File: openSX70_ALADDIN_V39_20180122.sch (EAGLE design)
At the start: 47 parts, among them J1 GND, Q1 5.8A/30V/35mΩ, Q2 5.8A/30V/35mΩ, U1 ATMEGA328P_TQFP, U3 BH1750FVI-TR, Y1 CSTCE16M0V53-R0

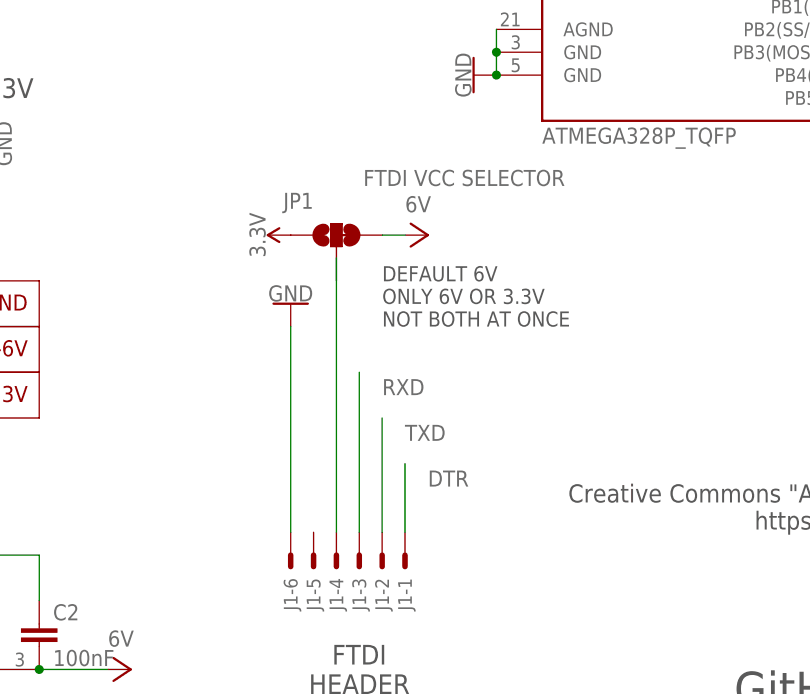
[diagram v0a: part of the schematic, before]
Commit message: New v.3.9 "Aladdin-fpc" is basically Aladdin with the FTDI header changed to the upper left in the form of a flexible cable.
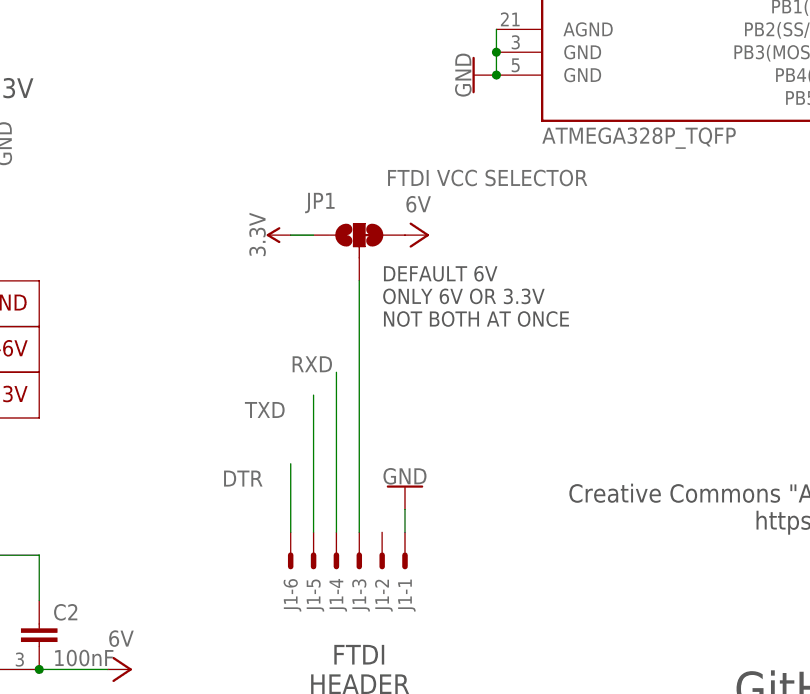
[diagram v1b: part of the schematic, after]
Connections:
- net DTR: now also J1-6.MS; no longer J1-1.MS
- net GND: now also J1-1.MS; no longer J1-6.MS
- net N$27: now also J1-3.MS, JP1.2; no longer J1-4.MS
- net RXD: now also J1-4.MS; no longer J1-3.MS
- net TXD: now also J1-5.MS; no longer J1-2.MS
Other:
- moved on the sheet: JP1
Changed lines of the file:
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@@
 <instance part="U1" gate="U$1" x="170.18" y="96.52"/>
 <instance part="SUPPLY1" gate="G$1" x="121.92" y="53.34" rot="R90"/>
-<instance part="GND1" gate="1" x="121.92" y="45.72" rot="R180"/>
+<instance part="GND1" gate="1" x="134.62" y="25.4" rot="R180"/>
 <instance part="GND2" gate="1" x="218.44" y="88.9" rot="R270"/>
 <instance part="P+1" gate="VCC" x="218.44" y="99.06" rot="R90"/>
@@
 <attribute name="VALUE" x="203.2" y="145.415" size="1.778" layer="96"/>
 </instance>
-<instance part="JP1" gate="G$1" x="127" y="53.34" smashed="yes" rot="R90">
-<attribute name="NAME" x="124.46" y="58.039" size="1.778" layer="95" font="vector" rot="R180"/>
-<attribute name="VALUE" x="152.4" y="58.801" size="1.778" layer="96" font="vector" rot="R180" align="top-left"/>
+<instance part="JP1" gate="G$1" x="129.54" y="53.34" smashed="yes" rot="R90">
+<attribute name="NAME" x="127" y="58.039" size="1.778" layer="95" font="vector" rot="R180"/>
+<attribute name="VALUE" x="154.94" y="58.801" size="1.778" layer="96" font="vector" rot="R180" align="top-left"/>
 </instance>
 <instance part="P+7" gate="VCC" x="137.16" y="53.34" rot="R270"/>
@@
 </segment>
 <segment>
-<pinref part="J1" gate="-3" pin="MS"/>
-<wire x1="129.54" y1="20.32" x2="129.54" y2="38.1" width="0.1524" layer="91"/>
-<label x="132.08" y="35.56" size="1.778" layer="95"/>
+<pinref part="J1" gate="-4" pin="MS"/>
+<wire x1="127" y1="20.32" x2="127" y2="38.1" width="0.1524" layer="91"/>
+<label x="121.92" y="38.1" size="1.778" layer="95"/>
 </segment>
 </net>
@@
 </segment>
 <segment>
-<pinref part="J1" gate="-2" pin="MS"/>
-<wire x1="132.08" y1="20.32" x2="132.08" y2="33.02" width="0.1524" layer="91"/>
-<label x="134.62" y="30.48" size="1.778" layer="95"/>
+<pinref part="J1" gate="-5" pin="MS"/>
+<wire x1="124.46" y1="20.32" x2="124.46" y2="35.56" width="0.1524" layer="91"/>
+<label x="116.84" y="33.02" size="1.778" layer="95"/>
 </segment>
 </net>
@@
 <pinref part="JP1" gate="G$1" pin="1"/>
 <pinref part="SUPPLY1" gate="G$1" pin="3.3V"/>
+<wire x1="124.46" y1="53.34" x2="121.92" y2="53.34" width="0.1524" layer="91"/>
 </segment>
 <segment>
@@
 </segment>
 <segment>
-<pinref part="GND1" gate="1" pin="GND"/>
-<wire x1="121.92" y1="20.32" x2="121.92" y2="43.18" width="0.1524" layer="91"/>
-<pinref part="J1" gate="-6" pin="MS"/>
-</segment>
-<segment>
 <pinref part="GND14" gate="1" pin="GND"/>
 <wire x1="119.38" y1="96.52" x2="124.46" y2="96.52" width="0.1524" layer="91"/>
@@
 <wire x1="73.66" y1="45.72" x2="76.2" y2="45.72" width="0.1524" layer="91"/>
 </segment>
+<segment>
+<pinref part="GND1" gate="1" pin="GND"/>
+<pinref part="J1" gate="-1" pin="MS"/>
+<wire x1="134.62" y1="22.86" x2="134.62" y2="20.32" width="0.1524" layer="91"/>
+</segment>
 </net>
 <net name="6V" class="0">
@@
 <pinref part="JP1" gate="G$1" pin="3"/>
 <pinref part="P+7" gate="VCC" pin="6V"/>
-<wire x1="134.62" y1="53.34" x2="132.08" y2="53.34" width="0.1524" layer="91"/>
 </segment>
 <segment>
@@
 </segment>
 <segment>
-<pinref part="J1" gate="-1" pin="MS"/>
-<wire x1="134.62" y1="20.32" x2="134.62" y2="27.94" width="0.1524" layer="91"/>
-<label x="137.16" y="25.4" size="1.778" layer="95"/>
+<pinref part="J1" gate="-6" pin="MS"/>
+<wire x1="121.92" y1="20.32" x2="121.92" y2="27.94" width="0.1524" layer="91"/>
+<label x="114.3" y="25.4" size="1.778" layer="95"/>
 </segment>
 </net>
@@
 <net name="N$27" class="0">
 <segment>
-<pinref part="J1" gate="-4" pin="MS"/>
-<wire x1="127" y1="20.32" x2="127" y2="50.8" width="0.1524" layer="91"/>
-</segment>
-</net>
+<pinref part="JP1" gate="G$1" pin="2"/>
+<pinref part="J1" gate="-3" pin="MS"/>
+<wire x1="129.54" y1="48.26" x2="129.54" y2="20.32" width="0.1524" layer="91"/>
+</segment>
+</net>

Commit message: Minor retouches
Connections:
- net S1: now also MISO.TP; no longer MOSI.TP
- net SOL2: now also MOSI.TP; no longer MISO.TP
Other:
- note added: "GitHub "aladdin-fpc" version"
- note removed: "GitHub "aladdin" version"
- moved on the sheet: MISO, MOSI
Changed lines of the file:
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@@
 <part name="P+9" library="openSX70" deviceset="VCC" device="" value="6V"/>
 <part name="GND4" library="SparkFun-PowerSymbols" library_urn="urn:adsk.eagle:library:530" deviceset="GND" device=""/>
+<part name="MOSI" library="testpad" library_urn="urn:adsk.eagle:library:385" deviceset="PTR1" device="TP08R" package3d_urn="urn:adsk.eagle:package:27956/1" value="PTR1TP08R"/>
 <part name="MISO" library="testpad" library_urn="urn:adsk.eagle:library:385" deviceset="PTR1" device="TP08R" package3d_urn="urn:adsk.eagle:package:27956/1" value="PTR1TP08R"/>
-<part name="MOSI" library="testpad" library_urn="urn:adsk.eagle:library:385" deviceset="PTR1" device="TP08R" package3d_urn="urn:adsk.eagle:package:27956/1" value="PTR1TP08R"/>
 <part name="SCK" library="testpad" library_urn="urn:adsk.eagle:library:385" deviceset="PTR1" device="TP08R" package3d_urn="urn:adsk.eagle:package:27956/1" value="PTR1TP08R"/>
 <part name="SDA" library="testpad" library_urn="urn:adsk.eagle:library:385" deviceset="PTR1" device="TP08R" package3d_urn="urn:adsk.eagle:package:27956/1" value="PTR1TP08R"/>
@@
 Creative Commons "Attribution-NonCommercial 4.0 International (CC BY-NC 4.0)"
 https://creativecommons.org/licenses/by-nc/4.0/</text>
-<text x="171.196" y="1.016" size="3.81" layer="97">GitHub "aladdin" version</text>
+<text x="171.196" y="1.016" size="3.81" layer="97">GitHub "aladdin-fpc" version</text>
 <text x="132.08" y="43.18" size="1.6764" layer="97">DEFAULT 6V
 ONLY 6V OR 3.3V
@@
 <attribute name="VALUE" x="70.866" y="45.72" size="1.778" layer="96" rot="R270" align="top-center"/>
 </instance>
-<instance part="MISO" gate="G$1" x="208.28" y="73.66" smashed="yes" rot="R90">
+<instance part="MOSI" gate="G$1" x="208.28" y="73.66" smashed="yes" rot="R90">
 <attribute name="NAME" x="220.98" y="74.676" size="1.778" layer="95" rot="R180"/>
 <attribute name="TP_SIGNAL_NAME" x="210.82" y="74.93" size="1.778" layer="97" rot="R90"/>
 </instance>
-<instance part="MOSI" gate="G$1" x="208.28" y="71.12" smashed="yes" rot="R90">
+<instance part="MISO" gate="G$1" x="208.28" y="71.12" smashed="yes" rot="R90">
 <attribute name="NAME" x="220.98" y="71.882" size="1.778" layer="95" rot="R180"/>
 <attribute name="TP_SIGNAL_NAME" x="210.82" y="72.39" size="1.778" layer="97" rot="R90"/>
@@
 <wire x1="193.04" y1="71.12" x2="205.74" y2="71.12" width="0.1524" layer="91"/>
 <label x="195.58" y="71.12" size="1.778" layer="95"/>
-<pinref part="MOSI" gate="G$1" pin="TP"/>
+<pinref part="MISO" gate="G$1" pin="TP"/>
 </segment>
 <segment>
@@
 <wire x1="193.04" y1="73.66" x2="205.74" y2="73.66" width="0.1524" layer="91"/>
 <label x="195.58" y="73.66" size="1.778" layer="95"/>
-<pinref part="MISO" gate="G$1" pin="TP"/>
-</segment>
-<segment>
+<pinref part="MOSI" gate="G$1" pin="TP"/>
+</segment>
+<segment>
